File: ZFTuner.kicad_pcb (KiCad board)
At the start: 2 copper layers, 159 parts, among them J101 RF_In, J102 RF_Out, J103 Tuner, J104 CAN, J201 SWD, J202 USB_C_Receptacle_USB2.0_16P, K401 HF3F-L-12-1ZL2T, K402 HF3F-L-12-1ZL2T, K403 HF3F-L-12-1ZL2T, K404 HF3F-L-12-1ZL2T, K405 HF3F-L-12-1ZL2T, K406 HF3F-L-12-1ZL2T, K407 HF3F-L-12-1ZL2T, K408 HF3F-L-12-1ZL2T, K501 HF3F-L-12-1ZL2T, K502 HF3F-L-12-1ZL2T, K503 HF3F-L-12-1ZL2T, K504 HF3F-L-12-1ZL2T, K505 HF3F-L-12-1ZL2T, K506 HF3F-L-12-1ZL2T, K507 HF3F-L-12-1ZL2T, Q401 PMOS, Q402 PMOS, Q403 NMOS, Q404 NMOS, Q501 PMOS, Q502 PMOS, Q503 NMOS, Q504 NMOS, SW201 CL-SB_22A-12T, U201 ULN2803A, U202 IP4234CZ6, U203 STM32G431CBTx, U204 MCP2542FDxMF, U205 ILD74, U301 LTC5507, U302 LTC5507, U601 HT7463A, U602 BD2243G, U603 MIC5504-3.3YM5, Y201 24MHz

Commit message: Placement of most components done
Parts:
- moved J104 215.9 mm to (267.0, 94.0), turned to -90 degrees
- moved J103 215.0 mm to (267.0, 108.0), turned to -90 degrees
- moved D601 175.3 mm to (266.8, 79.2)
- moved R602 171.6 mm to (265.0, 81.0)
- moved D201 165.5 mm to (252.2, 62.4)
- moved F201 162.3 mm to (258.7, 61.7)
- moved C209 158.6 mm to (259.0, 78.5)
- moved RV202 158.4 mm to (263.7, 60.7)
- moved R203 158.3 mm to (258.2, 49.7)
- moved J202 157.4 mm to (266.7, 54.2), turned to 90 degrees
- moved C210 157.2 mm to (257.8, 85.4)
- moved C205 157.1 mm to (254.0, 88.5)
- moved R202 156.5 mm to (258.7, 58.2)
- moved R208 155.6 mm to (260.0, 107.0), turned to -90 degrees
- moved RV201 153.2 mm to (258.7, 59.9), turned to 180 degrees
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
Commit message: PCB layout nearly done
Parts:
- moved Q504 80.6 mm to (208.4, 44.3), turned to 180 degrees
- moved Q502 79.0 mm to (204.2, 44.3), turned to 180 degrees
- moved R504 72.9 mm to (213.5, 44.3), turned to -90 degrees
- moved R506 70.5 mm to (211.5, 44.3), turned to 90 degrees
- moved R604 53.9 mm to (235.2, 60.0), turned to 180 degrees
- moved C607 53.9 mm to (238.7, 57.1)
- moved R606 53.8 mm to (232.2, 48.4)
- moved U602 53.7 mm to (233.1, 51.9)
- moved U603 53.7 mm to (235.6, 57.3)
- moved D603 53.6 mm to (230.2, 58.0)
- moved C606 53.6 mm to (232.4, 57.1)
- moved R605 52.0 mm to (229.4, 53.0)
- moved D602 49.7 mm to (239.7, 68.8), turned to 90 degrees
- moved C601 48.9 mm to (243.7, 73.4), turned to 90 degrees
- moved C603 47.5 mm to (234.5, 67.1), turned to -90 degrees
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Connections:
- net /Controller/USB_DM renamed /Controller/USB_DN
- net Net-(C417-Pad1) renamed /Capacitors_Bank/Cap1
- net Net-(C418-Pad1) renamed /Capacitors_Bank/Cap2
- net Net-(C419-Pad1) renamed /Capacitors_Bank/Cap3
- net Net-(C420-Pad1) renamed /Capacitors_Bank/Cap4
- net Net-(C421-Pad1) renamed /Capacitors_Bank/Cap5
- net Net-(C422-Pad1) renamed /Capacitors_Bank/Cap6
- net Net-(C423-Pad1) renamed /Capacitors_Bank/Cap7
- net Net-(K401-Pad11) renamed /Capacitors_Bank/Caps
- net Net-(K501-Pad14) renamed /Inductors_Bank/Ind1
- net Net-(K502-Pad14) renamed /Inductors_Bank/Ind2
- net Net-(K503-Pad14) renamed /Inductors_Bank/Ind3
- net Net-(K504-Pad14) renamed /Inductors_Bank/Ind4
- net Net-(K505-Pad14) renamed /Inductors_Bank/Ind5
- net Net-(K506-Pad14) renamed /Inductors_Bank/Ind6
- net Net-(U202-IO1b) renamed /Controller/CD_P
- net Net-(U202-IO2b) renamed /Controller/CD_N
- net Net-(U202-VP) renamed /Controller/USBC_VBUS
- C401 pad 1: /Capacitors_Bank/R4 -> /Capacitors_Bank/R1
- C401 pad 2: /Capacitors_Bank/Cap12v_2 -> /Capacitors_Bank/Cap12v_1
- C402 pad 1: /Capacitors_Bank/Cap12v_2 -> /Capacitors_Bank/Cap12v_1
- C402 pad 2: /Capacitors_Bank/S4 -> /Capacitors_Bank/S1
- C403 pad 1: /Capacitors_Bank/R1 -> /Capacitors_Bank/R2
- C404 pad 2: /Capacitors_Bank/S1 -> /Capacitors_Bank/S2
- C405 pad 1: /Capacitors_Bank/R2 -> /Capacitors_Bank/R3
- C406 pad 2: /Capacitors_Bank/S2 -> /Capacitors_Bank/S3
- C407 pad 1: /Capacitors_Bank/R3 -> /Capacitors_Bank/R4
- C408 pad 2: /Capacitors_Bank/S3 -> /Capacitors_Bank/S4
- C409 pad 1: /Capacitors_Bank/R4 -> /Capacitors_Bank/R1
- C409 pad 2: /Capacitors_Bank/Cap12v_1 -> /Capacitors_Bank/Cap12v_2
- C410 pad 1: /Capacitors_Bank/Cap12v_1 -> /Capacitors_Bank/Cap12v_2
- C410 pad 2: /Capacitors_Bank/S4 -> /Capacitors_Bank/S1
- C411 pad 1: /Capacitors_Bank/R1 -> /Capacitors_Bank/R2
- C412 pad 2: /Capacitors_Bank/S1 -> /Capacitors_Bank/S2
- C413 pad 1: /Capacitors_Bank/R2 -> /Capacitors_Bank/R3
- C414 pad 2: /Capacitors_Bank/S2 -> /Capacitors_Bank/S3
- C415 pad 1: /Capacitors_Bank/R3 -> /Capacitors_Bank/R4
- C416 pad 2: /Capacitors_Bank/S3 -> /Capacitors_Bank/S4
- C607 pad 2: +3V3 -> +3.3V
- D601 pad 2: +3V3 -> +3.3V
- J104 pad 1: /CAN_H -> /CAN_L
- J104 pad 2: /CAN_L -> /CAN_H
- K401 pad 12: /Capacitors_Bank/RF_In -> /RF_Out
- K401 pad 14: /RF_Out -> /Capacitors_Bank/RF_In
- K401 pad A1: /Capacitors_Bank/S4 -> /Capacitors_Bank/S1
- K401 pad A2: /Capacitors_Bank/R4 -> /Capacitors_Bank/R1
- K401 pad A3: /Capacitors_Bank/Cap12v_2 -> /Capacitors_Bank/Cap12v_1
- K402 pad A1: /Capacitors_Bank/S1 -> /Capacitors_Bank/S2
- K402 pad A2: /Capacitors_Bank/R1 -> /Capacitors_Bank/R2
- K403 pad A1: /Capacitors_Bank/S2 -> /Capacitors_Bank/S3
- K403 pad A2: /Capacitors_Bank/R2 -> /Capacitors_Bank/R3
- K404 pad A1: /Capacitors_Bank/S3 -> /Capacitors_Bank/S4
- K404 pad A2: /Capacitors_Bank/R3 -> /Capacitors_Bank/R4
- K405 pad A1: /Capacitors_Bank/S4 -> /Capacitors_Bank/S1
- K405 pad A2: /Capacitors_Bank/R4 -> /Capacitors_Bank/R1
- K405 pad A3: /Capacitors_Bank/Cap12v_1 -> /Capacitors_Bank/Cap12v_2
- K406 pad A1: /Capacitors_Bank/S1 -> /Capacitors_Bank/S2
- K406 pad A2: /Capacitors_Bank/R1 -> /Capacitors_Bank/R2
- K407 pad A1: /Capacitors_Bank/S2 -> /Capacitors_Bank/S3
- K407 pad A2: /Capacitors_Bank/R2 -> /Capacitors_Bank/R3
- K408 pad A1: /Capacitors_Bank/S3 -> /Capacitors_Bank/S4
- K408 pad A2: /Capacitors_Bank/R3 -> /Capacitors_Bank/R4
- R403 pad 2: /Capacitors_Bank/CapRels_1 -> /Controller/CapRels_1
- R404 pad 2: /Capacitors_Bank/CapRels_2 -> /Controller/CapRels_2
- R503 pad 2: /Inductors_Bank/IndRels_1 -> /Controller/IndRels_1
- R504 pad 2: /Inductors_Bank/IndRels_2 -> /Controller/IndRels_2
- U201 pad 1: Net-(U201-I1) -> /Controller/S1
- U201 pad 2: Net-(U201-I2) -> /Controller/R1
- U201 pad 3: Net-(U201-I3) -> /Controller/S2
- U201 pad 4: Net-(U201-I4) -> /Controller/R2
- U201 pad 5: Net-(U201-I5) -> /Controller/S3
- U201 pad 6: Net-(U201-I6) -> /Controller/R3
- U201 pad 7: Net-(U201-I7) -> /Controller/S4
- U201 pad 8: Net-(U201-I8) -> /Controller/R4
- U203 pad 10: Net-(U201-I1) -> /Controller/R4
- U203 pad 11: Net-(U201-I2) -> /Controller/S4
- U203 pad 12: Net-(U201-I3) -> /Controller/R3
- U203 pad 13: Net-(U201-I4) -> /Controller/S3
- U203 pad 14: Net-(U201-I5) -> /Controller/R2
- U203 pad 15: Net-(U201-I6) -> /Controller/S2
- U203 pad 30: Net-(U201-I7) -> /Controller/R1
- U203 pad 31: Net-(U201-I8) -> /Controller/S1
- U603 pad 5: +3V3 -> +3.3V
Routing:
- net /Capacitors_Bank/R1: track 0.00 -> 381.7 mm, vias 0 -> 5
- net /Capacitors_Bank/S1: track 0.00 -> 371.7 mm, vias 0 -> 4
- net /Capacitors_Bank/R2: track 0.00 -> 344.9 mm, vias 0 -> 4
- net /Capacitors_Bank/S2: track 0.00 -> 340.9 mm, vias 0 -> 4
- net /Capacitors_Bank/R3: track 0.00 -> 308.7 mm, vias 0 -> 4
- net /Capacitors_Bank/S3: track 0.00 -> 301.5 mm, vias 0 -> 4
- net /Capacitors_Bank/S4: track 0.00 -> 256.9 mm, vias 0 -> 3
- net /Capacitors_Bank/R4: track 0.00 -> 256.2 mm, vias 0 -> 1
- net +3.3V: track 0.00 -> 241.1 mm, vias 0 -> 17
- net /Controller/~{SWR_SHDN}: track 0.00 -> 205.9 mm, vias 0 -> 3
- net /Controller/Fwd_V: track 0.00 -> 192.5 mm, vias 0 -> 2
- net /Controller/Rfl_V: track 0.00 -> 176.2 mm, vias 0 -> 2
- net /RF_Out: track 0.00 -> 175.3 mm
- net /Capacitors_Bank/Cap12v_1: track 0.00 -> 155.3 mm
- net /Capacitors_Bank/Cap12v_2: track 0.00 -> 155.2 mm
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- added copper zone on F.Cu, net +12V
- added copper zone on In1.Cu, net +12V
- added copper zone on In2.Cu, net +12V
- added copper zone on F.Cu, net +3.3V
- added copper zone on In1.Cu, net +3.3V
- added copper zone on F.Cu, net +5.4V
- added copper zone on F.Cu, net /Controller/USBC_VBUS
- added copper zone on F.Cu, net /Power/5V_SW
- added copper zone on B.Cu, net GNDD
- added copper zone on F.Cu, net GNDD
- added copper zone on In1.Cu, net GNDD
- added copper zone on In2.Cu, net GNDD
- added copper zone on B.Cu, net GNDPWR
- added copper zone on F.Cu, net GNDPWR
- added copper zone on In1.Cu, net GNDPWR
- added copper zone on In2.Cu, net GNDPWR
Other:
- board outline added: 221.9 x 82 mm
- copper layers 2 -> 4
- board text added: "13.8V"
- board text added: "CAN"
- board text added: "GND"
- board text added: "H"
- board text added: "KEY"
- board text added: "L"
- board text added: "START"
- board text added: "SWD"
- board text added: "USB"

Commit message: Everything is connected
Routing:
- net /Controller/SWDIO: track 0.00 -> 67.3 mm, vias 0 -> 2
- net /Controller/SWCLK: track 0.00 -> 64.3 mm, vias 0 -> 2
- net /Controller/SWO: track 0.00 -> 58.1 mm, vias 0 -> 2
- net /Controller/UC_Reset: track 1.75 -> 54.2 mm, vias 0 -> 2
- net /Controller/START: track 2.50 -> 32.9 mm, vias 0 -> 2
- net +5.4V: track 31.9 -> 55.5 mm, vias 0 -> 1
- net Net-(R209-Pad2): track 0.00 -> 13.8 mm, vias 0 -> 2
- net Net-(R207-Pad2): track 0.00 -> 2.70 mm
- net /Capacitors_Bank/R3: track 308.7 -> 307.4 mm
- net /Capacitors_Bank/R4: track 256.2 -> 255.2 mm
- net /Capacitors_Bank/S4: track 256.9 -> 255.9 mm
- net /Capacitors_Bank/S3: track 301.5 -> 300.8 mm
- net GNDD: vias 0 -> 17
- net GND: vias 0 -> 6
- added copper zone on B.Cu, net GND
- added copper zone on F.Cu, net GND
- added copper zone on In1.Cu, net GND
- added copper zone on In2.Cu, net GND

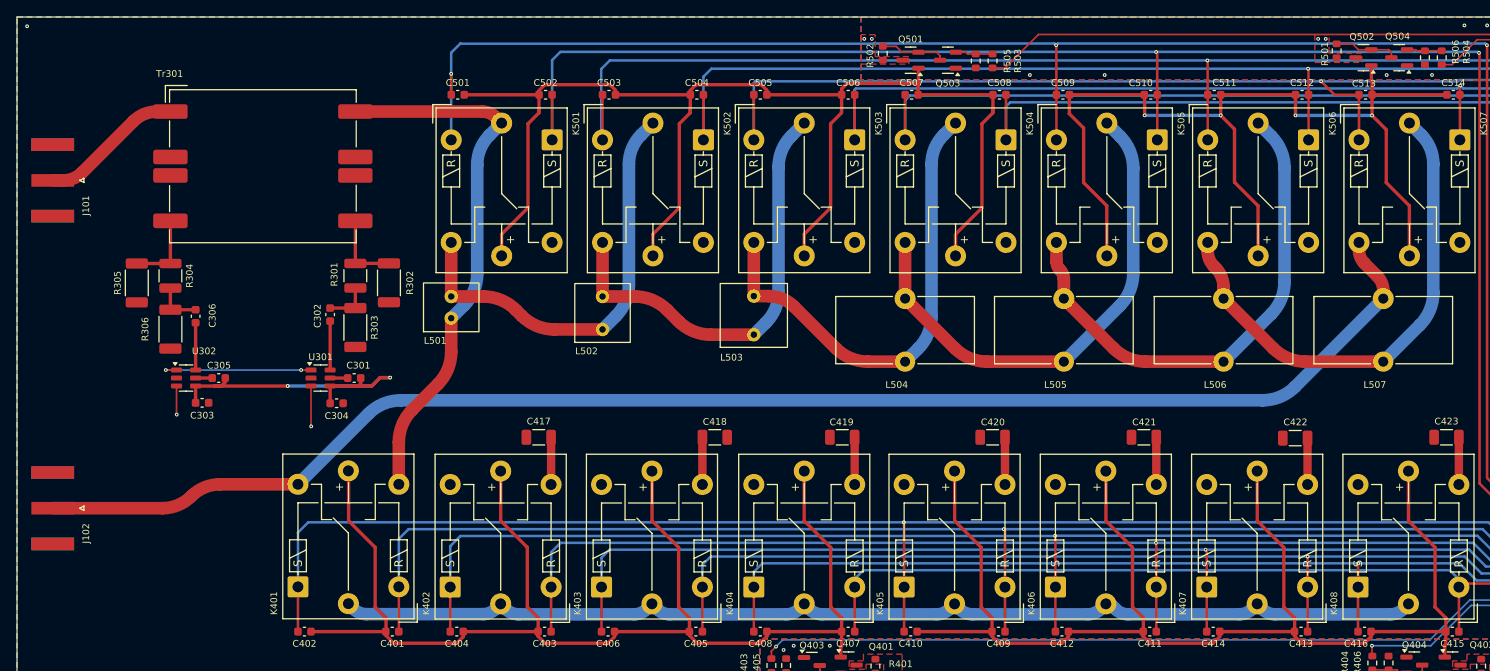
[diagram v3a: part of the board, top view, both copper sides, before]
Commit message: Adjusted some traces
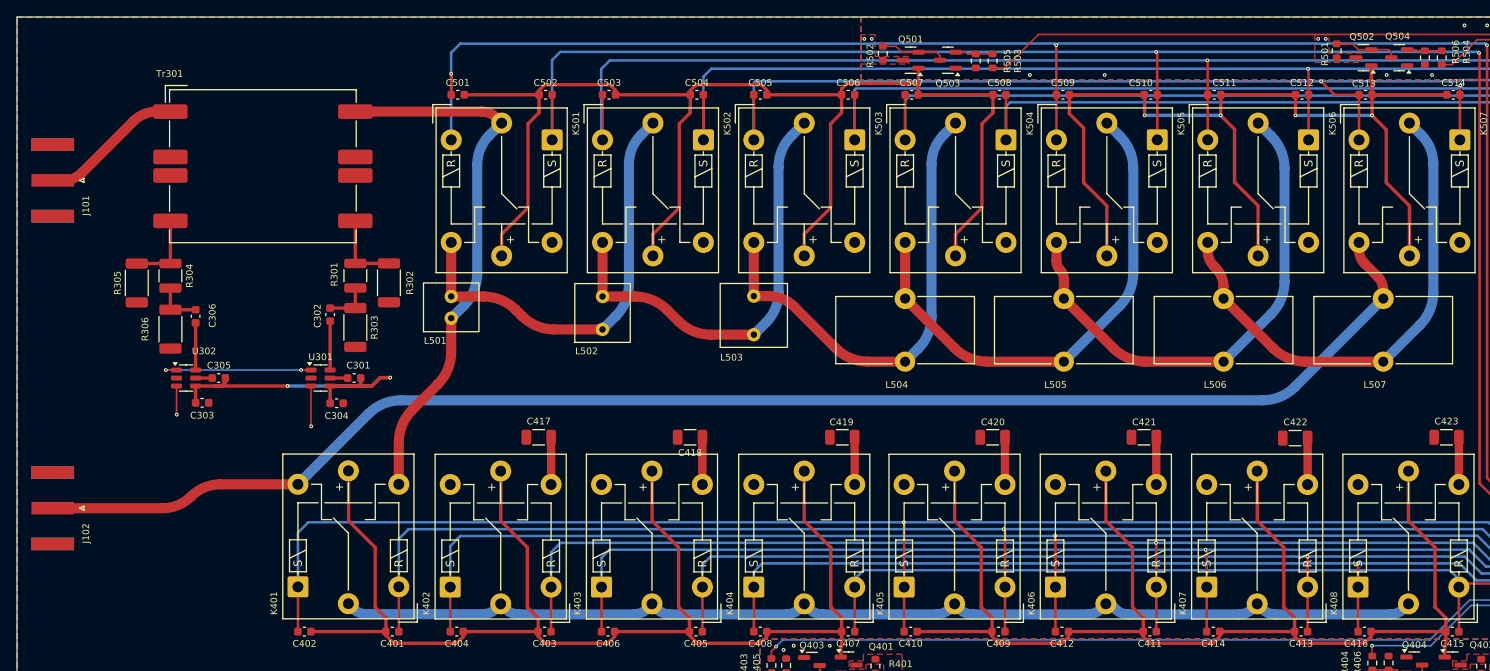
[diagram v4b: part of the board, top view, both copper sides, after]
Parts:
- moved C418 2.94 mm to (124.1, 89.5), turned to 180 degrees
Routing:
- net GND: vias 6 -> 5

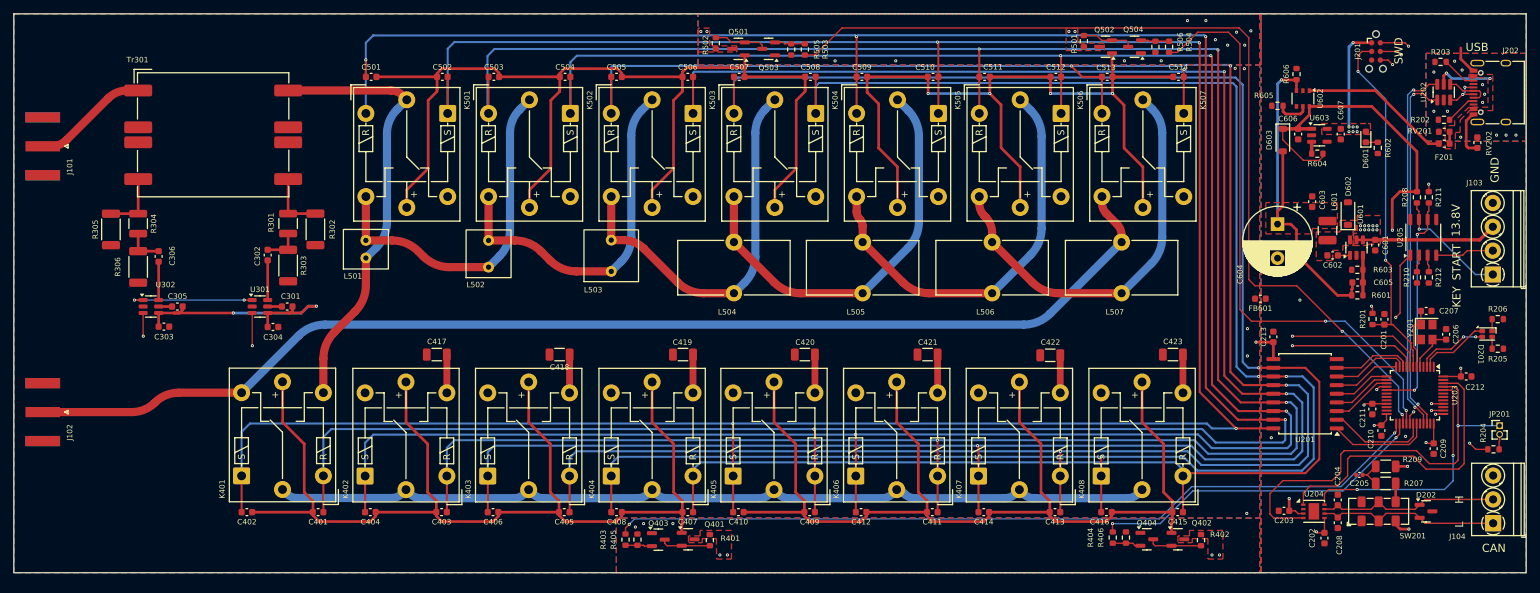
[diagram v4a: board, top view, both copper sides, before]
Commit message: Many more vias, improved some routing
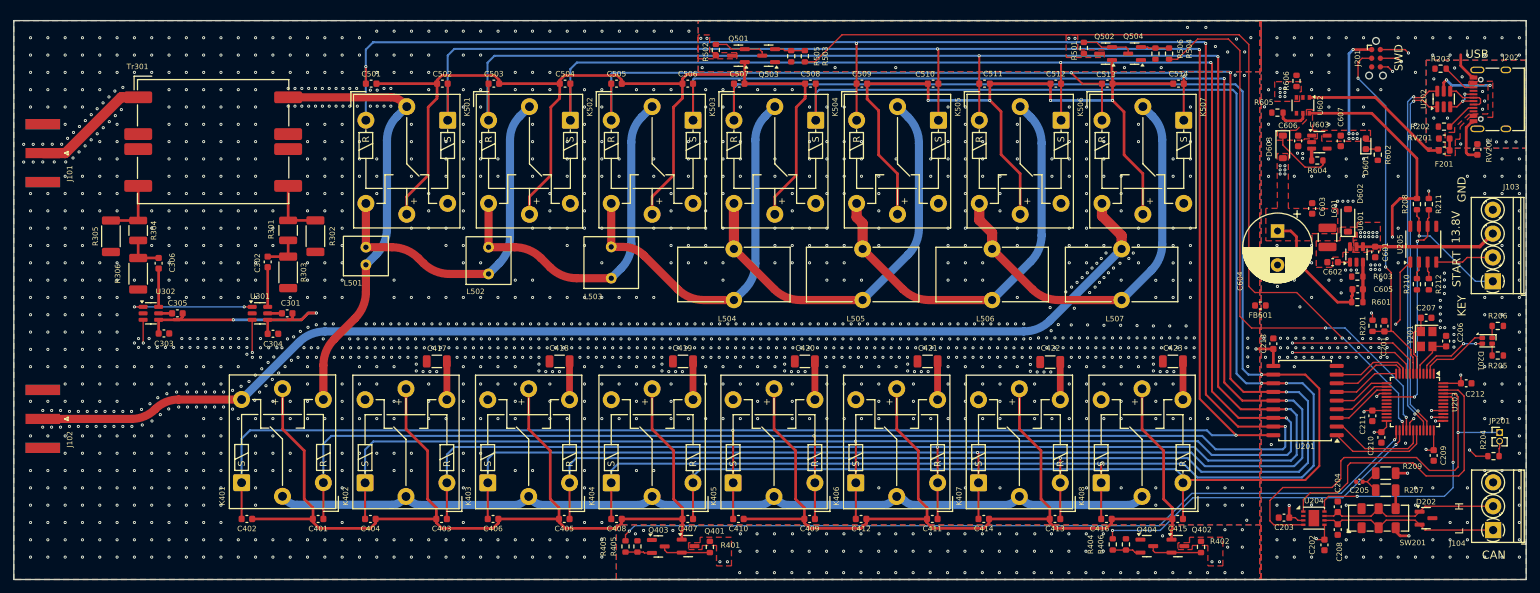
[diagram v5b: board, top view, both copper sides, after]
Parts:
- moved C201 1.00 mm to (245.1, 85.3)
- moved C202 1.00 mm to (236.3, 117.4)
- moved C203 1.00 mm to (230.4, 113.4)
- moved C204 1.00 mm to (238.2, 111.8)
- moved C205 1.00 mm to (241.4, 108.2)
- moved C206 1.00 mm to (254.2, 87.5)
- moved C207 1.00 mm to (251.2, 84.1)
- moved C208 1.00 mm to (238.2, 115.2)
- moved C209 1.00 mm to (252.3, 104.3)
- moved C210 1.00 mm to (244.7, 101.7)
- moved C211 1.00 mm to (243.3, 98.5)
- moved C212 1.00 mm to (257.1, 93.7)
- moved C213 1.00 mm to (228.8, 87.9)
- moved C301 1.00 mm to (84.1, 83.5)
- moved C302 1.00 mm to (81.2, 75.9)
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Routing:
- net +5.4V: track 55.5 -> 19.3 mm, vias 1 -> 12
- net +5V: track 105.1 -> 96.9 mm
- net GNDPWR: vias 12 -> 13
- net GNDD: vias 17 -> 320
- net GND: vias 5 -> 1509
- added copper zone on In2.Cu, net +5.4V
- added copper zone on F.Cu, net +5V

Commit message: More layout polishing
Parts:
- moved F201 14.8 mm to (253.3, 44.8)
- moved RV201 11.4 mm to (253.3, 46.5)
- moved R203 0.70 mm to (253.3, 48.2)
- moved J104 0.15 mm to (260.9, 115.2)
- moved Y201 0.15 mm to (251.4, 87.2)
- moved C207 0.10 mm to (251.3, 84.1)
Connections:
- net /Controller/R1 renamed /Controller/C_R1
- net /Controller/R2 renamed /Controller/C_R2
- net /Controller/R3 renamed /Controller/C_R3
- net /Controller/R4 renamed /Controller/C_R4
- net /Controller/S1 renamed /Controller/C_S1
- net /Controller/S2 renamed /Controller/C_S2
- net /Controller/S3 renamed /Controller/C_S3
- net /Controller/S4 renamed /Controller/C_S4
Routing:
- net +12V: track 71.3 -> 23.1 mm, vias 19 -> 15
- net /Controller/START: track 32.9 -> 64.6 mm
- net VBUS: track 22.2 -> 26.8 mm
- net /Controller/USBC_VBUS: track 10.3 -> 8.22 mm
- net /Controller/Op_LED: track 10.5 -> 12.5 mm
- net /Controller/CAN_STBY: track 35.9 -> 37.9 mm
- net +5.4V: track 19.3 -> 18.2 mm
- net /Controller/USB_DP: track 53.6 -> 54.5 mm
- net +5V: track 96.9 -> 96.1 mm
- net +3.3V: track 241.4 -> 242.1 mm, vias 17 -> 23
- net /Controller/XTAL_2: track 9.31 -> 8.62 mm
- net /Controller/CAN_TX: track 44.5 -> 45.0 mm
- net GNDD: track 11.0 -> 11.3 mm, vias 320 -> 370
- net /Controller/Error_LED: vias 2 -> 0
- net GNDPWR: vias 13 -> 11
- added copper zone on In2.Cu, net +3.3V
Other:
- board text added: "RF In"
- board text added: "RF Out"
- board text added: "ZFTuner ${REVISION}"
